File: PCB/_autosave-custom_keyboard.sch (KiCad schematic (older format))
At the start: 397 parts, among them IC1 FE2.1, J1 USB_A, J2 USB_A, J3 USB_A, J4 Conn_01x08_Male, SW1 SW_Push, U1 PRTR5V0U2X, U2 24LC02, U3 PRTR5V0U2X, U4 PRTR5V0U2X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

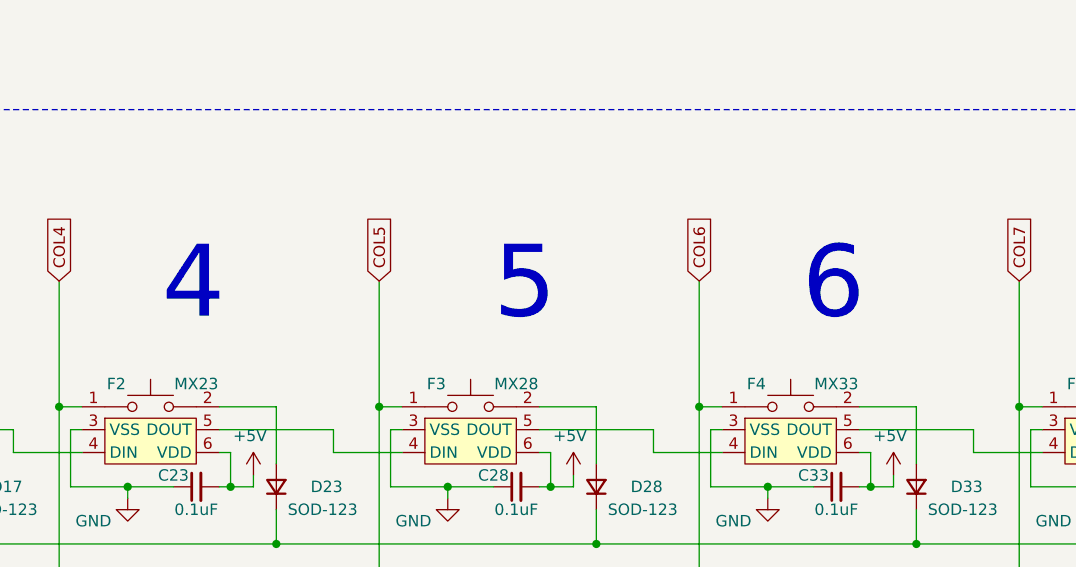
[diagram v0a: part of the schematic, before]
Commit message: Placed resistors and capacitators
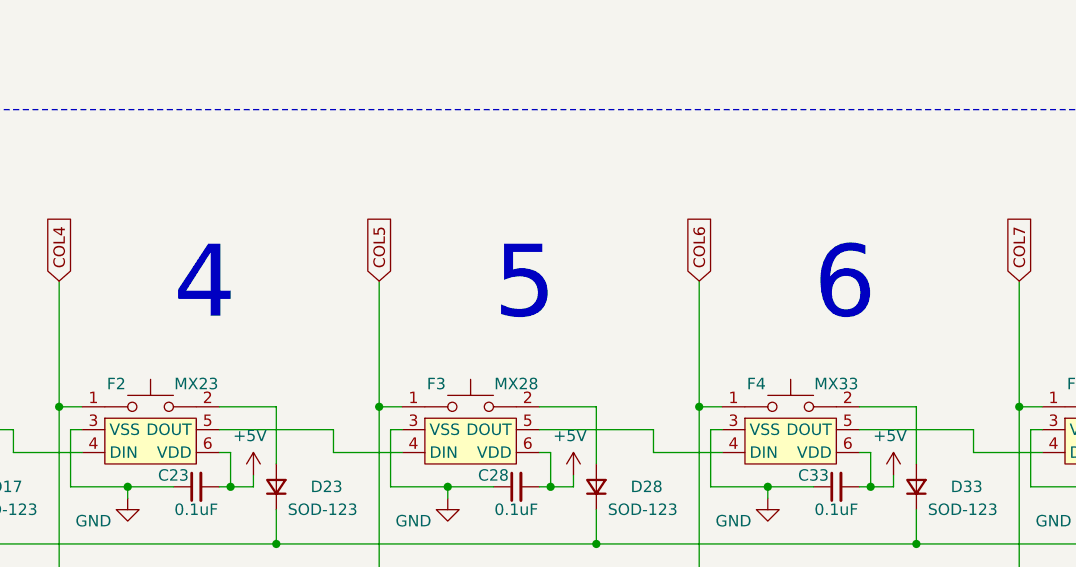
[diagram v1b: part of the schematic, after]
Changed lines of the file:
@@
 Text Notes 13900 3550 0    315  ~ 0
 7
-Text Notes 12350 3550 0    315  ~ 0
+Text Notes 12400 3550 0    315  ~ 0
 6
 Text Notes 11000 3550 0    315  ~ 0
 5
-Text Notes 9550 3550 0    315  ~ 0
+Text Notes 9600 3550 0    315  ~ 0
 4
 Text Notes 8300 3550 0    315  ~ 0
